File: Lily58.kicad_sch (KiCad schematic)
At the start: 40 parts, among them J1 USB_C_Receptacle, J2 USB_C_Receptacle, J3 Conn_01x03_Pin, U1 BQ24091DGQ, U2 TPS63000, U3 TPS63000

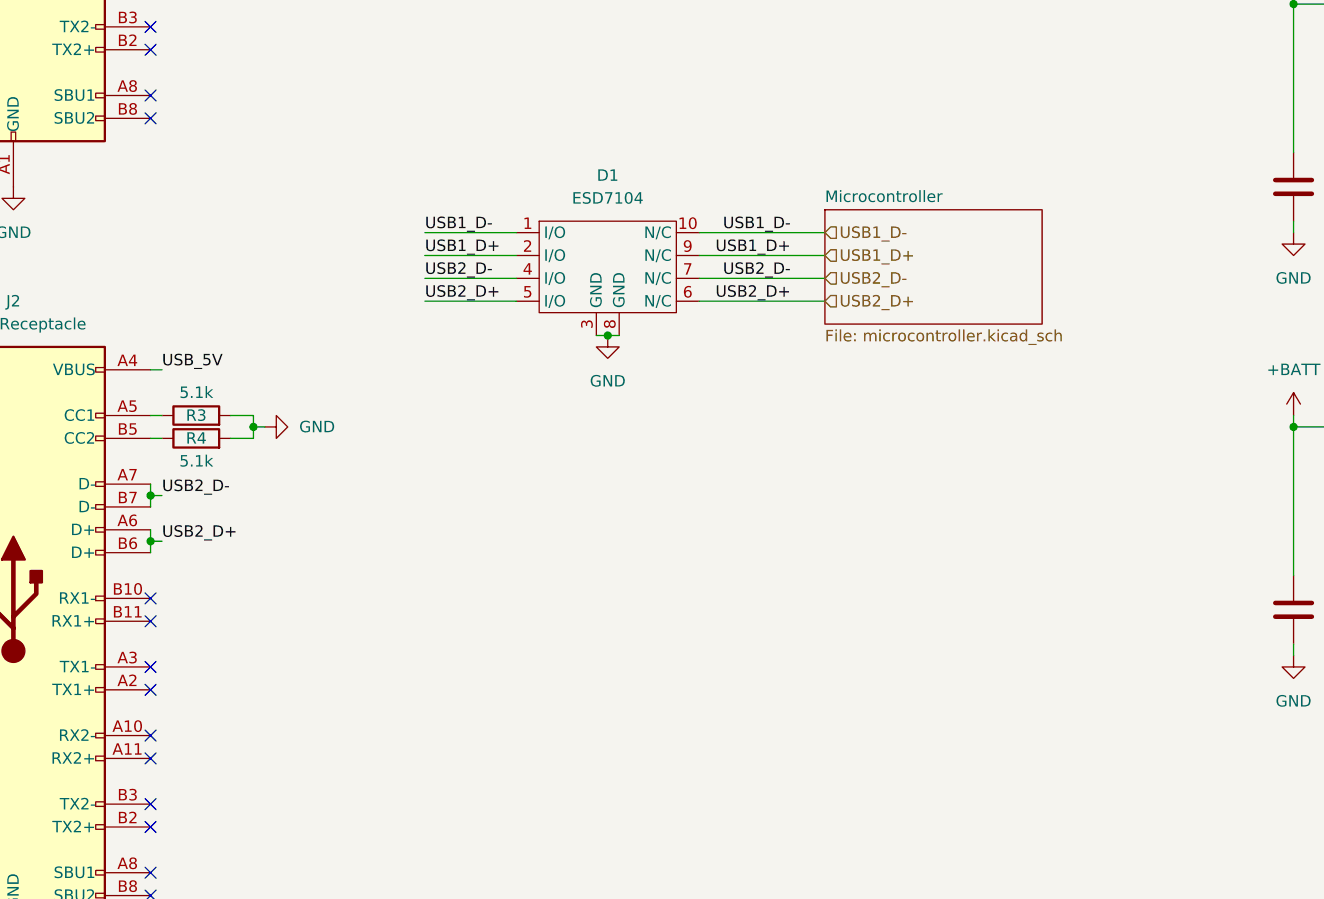
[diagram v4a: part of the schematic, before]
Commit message: completed ESP32-S3 circuit
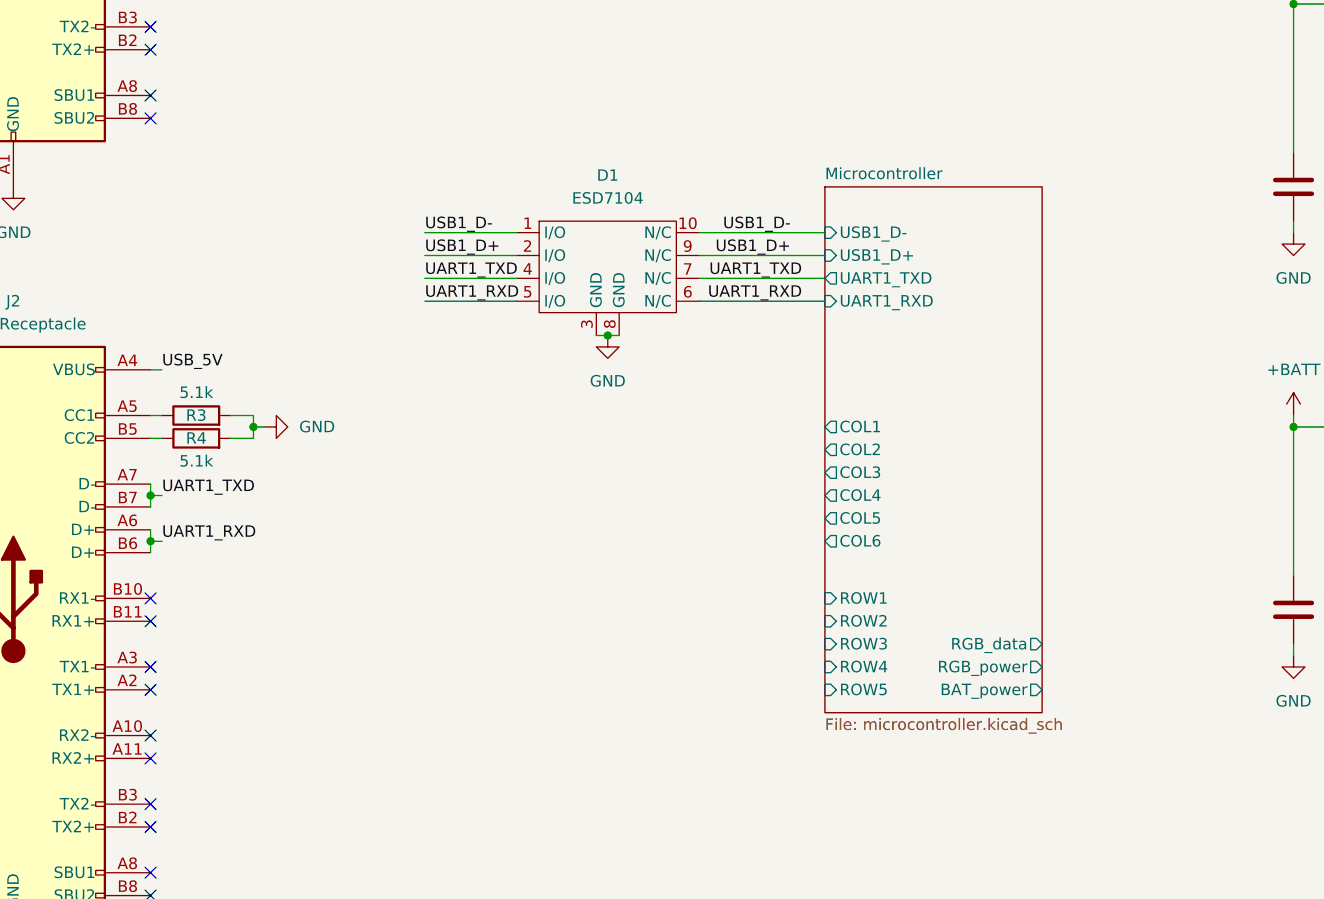
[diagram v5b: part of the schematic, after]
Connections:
- net USB2_D+ renamed UART1_RXD
- net USB2_D- renamed UART1_TXD
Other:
- sheet Microcontroller ports: added BAT_power, COL1, COL2, COL3, COL4, COL5, COL6, RGB_data, RGB_power, ROW1, ROW2, ROW3, ROW4, ROW5, UART1_RXD, UART1_TXD, USB1_D+, USB1_D-; removed none
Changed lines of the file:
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@@
     (effects (font (size 1.27 1.27)) (justify left bottom))
   )
-  (label "USB2_D-" (at 45.72 132.08 0) (fields_autoplaced)
+  (label "UART1_TXD" (at 45.72 132.08 0) (fields_autoplaced)
     (effects (font (size 1.27 1.27)) (justify left bottom))
   )
@@
     (effects (font (size 1.27 1.27)) (justify right bottom))
   )
-  (label "USB2_D+" (at 115.57 110.49 180) (fields_autoplaced)
+  (label "UART1_RXD" (at 116.84 110.49 180) (fields_autoplaced)
     (effects (font (size 1.27 1.27)) (justify right bottom))
   )
@@
     (effects (font (size 1.27 1.27)) (justify right bottom))
   )
-  (label "USB2_D-" (at 115.57 107.95 180) (fields_autoplaced)
+  (label "UART1_TXD" (at 116.84 107.95 180) (fields_autoplaced)
     (effects (font (size 1.27 1.27)) (justify right bottom))
   )
@@
     (effects (font (size 1.27 1.27)) (justify left bottom))
   )
-  (label "USB2_D-" (at 74.93 107.95 0) (fields_autoplaced)
+  (label "UART1_TXD" (at 74.93 107.95 0) (fields_autoplaced)
     (effects (font (size 1.27 1.27)) (justify left bottom))
   )
@@
     (effects (font (size 1.27 1.27)) (justify left bottom))
   )
-  (label "USB2_D+" (at 45.72 137.16 0) (fields_autoplaced)
+  (label "UART1_RXD" (at 45.72 137.16 0) (fields_autoplaced)
     (effects (font (size 1.27 1.27)) (justify left bottom))
   )
@@
     (effects (font (size 1.27 1.27)) (justify left bottom))
   )
-  (label "USB2_D+" (at 74.93 110.49 0) (fields_autoplaced)
+  (label "UART1_RXD" (at 74.93 110.49 0) (fields_autoplaced)
     (effects (font (size 1.27 1.27)) (justify left bottom))
-  )
-  (hierarchical_label "USB2_D-" (shape input) (at 119.38 107.95 0) (fields_autoplaced)
-    (effects (font (size 1.27 1.27)) (justify left))
-  )
-  (hierarchical_label "USB1_D-" (shape input) (at 119.38 102.87 0) (fields_autoplaced)
-    (effects (font (size 1.27 1.27)) (justify left))
-  )
-  (hierarchical_label "USB1_D+" (shape input) (at 119.38 105.41 0) (fields_autoplaced)
-    (effects (font (size 1.27 1.27)) (justify left))
-  )
-  (hierarchical_label "USB2_D+" (shape input) (at 119.38 110.49 0) (fields_autoplaced)
-    (effects (font (size 1.27 1.27)) (justify left))
   )
   (symbol (lib_id "power:GND") (at 215.9 102.87 0) (unit 1)
@@
     )
   )
-  (sheet (at 119.38 100.33) (size 24.13 12.7) (fields_autoplaced)
+  (sheet (at 119.38 97.79) (size 24.13 58.42) (fields_autoplaced)
     (stroke (width 0.1524) (type solid))
     (fill (color 0 0 0 0.0000))
-    (property "Sheetname" "Microcontroller" (at 119.38 99.6184 0)
+    (property "Sheetname" "Microcontroller" (at 119.38 97.0784 0)
       (effects (font (size 1.27 1.27)) (justify left bottom))
     )
-    (property "Sheetfile" "microcontroller.kicad_sch" (at 119.38 113.6146 0)
+    (property "Sheetfile" "microcontroller.kicad_sch" (at 119.38 156.7946 0)
       (effects (font (size 1.27 1.27)) (justify left top))
     )
-    (instances
+    (pin "ROW1" input (at 119.38 143.51 180)
+      (effects (font (size 1.27 1.27)) (justify left))
+    )
+    (pin "COL5" output (at 119.38 134.62 180)
+      (effects (font (size 1.27 1.27)) (justify left))
+    )
+    (pin "COL4" output (at 119.38 132.08 180)
+      (effects (font (size 1.27 1.27)) (justify left))
+    )
+    (pin "COL3" output (at 119.38 129.54 180)
+      (effects (font (size 1.27 1.27)) (justify left))
+    )
+    (pin "ROW3" input (at 119.38 148.59 180)
+      (effects (font (size 1.27 1.27)) (justify left))
+    )
+    (pin "ROW4" input (at 119.38 151.13 180)
+      (effects (font (size 1.27 1.27)) (justify left))
+    )
+    (pin "ROW2" input (at 119.38 146.05 180)
+      (effects (font (size 1.27 1.27)) (justify left))
+    )
+    (pin "COL2" output (at 119.38 127 180)
+      (effects (font (size 1.27 1.27)) (justify left))
+    )
+    (pin "COL1" output (at 119.38 124.46 180)
+      (effects (font (size 1.27 1.27)) (justify left))
+    )
+    (pin "USB1_D+" input (at 119.38 105.41 180)
+      (effects (font (size 1.27 1.27)) (justify left))
+    )
+    (pin "USB1_D-" input (at 119.38 102.87 180)
+      (effects (font (size 1.27 1.27)) (justify left))
+    )
+    (pin "UART1_RXD" input (at 119.38 110.49 180)
+      (effects (font (size 1.27 1.27)) (justify left))
+    )
+    (pin "UART1_TXD" output (at 119.38 107.95 180)
+      (effects (font (size 1.27 1.27)) (justify left))
+    )
+    (pin "COL6" output (at 119.38 137.16 180)
+      (effects (font (size 1.27 1.27)) (justify left))
+    )
+    (pin "ROW5" input (at 119.38 153.67 180)
+      (effects (font (size 1.27 1.27)) (justify left))
+    )
+    (pin "RGB_power" output (at 143.51 151.13 0)
+      (effects (font (size 1.27 1.27)) (justify right))
+    )
+    (pin "RGB_data" output (at 143.51 148.59 0)
+      (effects (font (size 1.27 1.27)) (justify right))
+    )
+    (pin "BAT_power" output (at 143.51 153.67 0)
+      (effects (font (size 1.27 1.27)) (justify right))
+    )
+    (instances

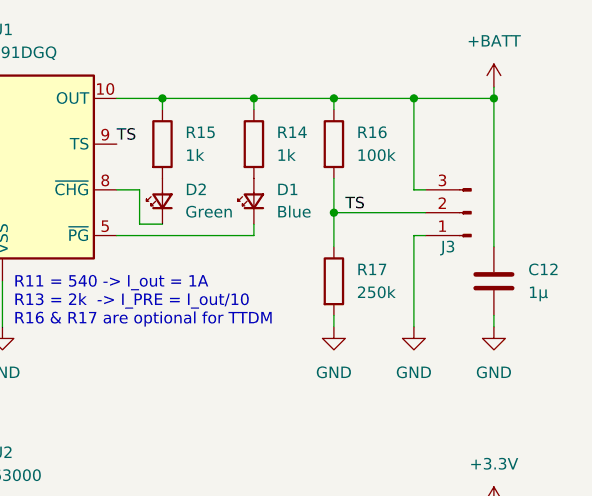
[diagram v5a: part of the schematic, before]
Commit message: added power switch
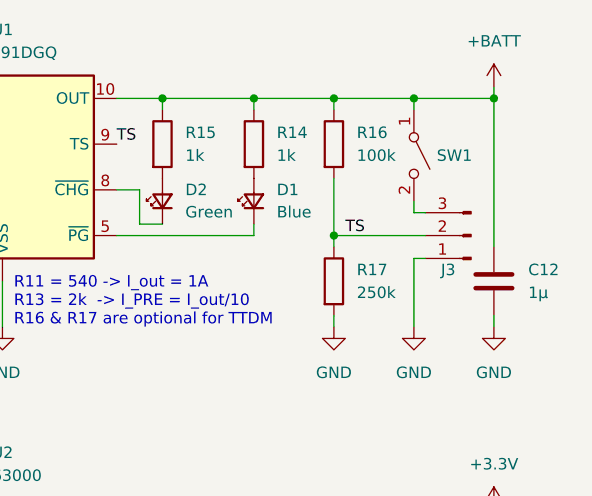
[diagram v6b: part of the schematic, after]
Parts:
- added SW1: SW_SPST, symbol Switch:SW_SPST
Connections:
- net +BATT: now also SW1.1 (A); no longer J3.3 (Pin_3)
- new net: J3.3 (Pin_3), SW1.2 (B)
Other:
- moved on the sheet: J3
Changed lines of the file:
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@@
   (junction (at 236.22 77.47) (diameter 0) (color 0 0 0 0)
   )
+  (junction (at 254 45.72) (diameter 0) (color 0 0 0 0)
+  )
   (junction (at 181.61 137.16) (diameter 0) (color 0 0 0 0)
   )
@@
   )
   (junction (at 236.22 124.46) (diameter 0) (color 0 0 0 0)
-  )
-  (junction (at 254 43.18) (diameter 0) (color 0 0 0 0)
   )
   (junction (at 236.22 137.16) (diameter 0) (color 0 0 0 0)
@@
     (stroke (width 0) (type default))
   )
-  (wire (pts (xy 262.89 40.64) (xy 264.16 40.64))
+  (wire (pts (xy 262.89 43.18) (xy 264.16 43.18))
     (stroke (width 0) (type default))
   )
@@
     (stroke (width 0) (type default))
   )
-  (wire (pts (xy 254 43.18) (xy 254 46.99))
-    (stroke (width 0) (type default))
-  )
   (wire (pts (xy 245.11 31.75) (xy 245.11 30.48))
     (stroke (width 0) (type default))
@@
     (stroke (width 0) (type default))
   )
+  (wire (pts (xy 262.89 41.91) (xy 262.89 43.18))
+    (stroke (width 0) (type default))
+  )
   (wire (pts (xy 247.65 90.17) (xy 236.22 90.17))
     (stroke (width 0) (type default))
@@
     (stroke (width 0) (type default))
   )
-  (wire (pts (xy 254 39.37) (xy 254 43.18))
+  (wire (pts (xy 254 39.37) (xy 254 45.72))
     (stroke (width 0) (type default))
   )
@@
     (stroke (width 0) (type default))
   )
-  (wire (pts (xy 262.89 45.72) (xy 264.16 45.72))
+  (wire (pts (xy 262.89 48.26) (xy 264.16 48.26))
     (stroke (width 0) (type default))
   )
@@
     (stroke (width 0) (type default))
   )
-  (wire (pts (xy 262.89 45.72) (xy 262.89 55.88))
+  (wire (pts (xy 262.89 48.26) (xy 262.89 55.88))
     (stroke (width 0) (type default))
   )
@@
     (stroke (width 0) (type default))
   )
-  (wire (pts (xy 254 43.18) (xy 264.16 43.18))
+  (wire (pts (xy 254 45.72) (xy 264.16 45.72))
     (stroke (width 0) (type default))
   )
@@
     (stroke (width 0) (type default))
   )
+  (wire (pts (xy 254 45.72) (xy 254 46.99))
+    (stroke (width 0) (type default))
+  )
   (wire (pts (xy 55.88 39.37) (xy 53.34 39.37))
     (stroke (width 0) (type default))
   )
-  (wire (pts (xy 262.89 30.48) (xy 262.89 40.64))
+  (wire (pts (xy 262.89 30.48) (xy 262.89 31.75))
     (stroke (width 0) (type default))
   )
@@
     (effects (font (size 1.27 1.27)) (justify left bottom))
   )
-  (label "TS" (at 255.27 43.18 0) (fields_autoplaced)
+  (label "TS" (at 255.27 45.72 0) (fields_autoplaced)
     (effects (font (size 1.27 1.27)) (justify left bottom))
   )
@@
     )
   )
-  (symbol (lib_id "Connector:Conn_01x03_Pin") (at 269.24 43.18 180) (unit 1)
+  (symbol (lib_id "Connector:Conn_01x03_Pin") (at 269.24 45.72 180) (unit 1)
     (in_bom yes) (on_board yes) (dnp no)
-    (property "Reference" "J3" (at 266.7 46.99 0)
-      (effects (font (size 1.27 1.27)))
-    )
-    (property "Value" "Conn_01x03_Pin" (at 268.605 48.26 0)
-      (effects (font (size 1.27 1.27)) hide)
-    )
-    (property "Footprint" "" (at 269.24 43.18 0)
-      (effects (font (size 1.27 1.27)) hide)
-    )
-    (property "Datasheet" "~" (at 269.24 43.18 0)
+    (property "Reference" "J3" (at 266.7 49.53 0)
+      (effects (font (size 1.27 1.27)))
+    )
+    (property "Value" "Conn_01x03_Pin" (at 268.605 50.8 0)
+      (effects (font (size 1.27 1.27)) hide)
+    )
+    (property "Footprint" "" (at 269.24 45.72 0)
+      (effects (font (size 1.27 1.27)) hide)
+    )
+    (property "Datasheet" "~" (at 269.24 45.72 0)
       (effects (font (size 1.27 1.27)) hide)
     )
@@
         )
       )
+    )
+  )
+  (symbol (lib_id "Switch:SW_SPST") (at 262.89 36.83 270) (unit 1)
+    (in_bom yes) (on_board yes) (dnp no) (fields_autoplaced)
+    (property "Reference" "SW1" (at 265.43 36.83 90)
+      (effects (font (size 1.27 1.27)) (justify left))
+    )
+    (property "Value" "SW_SPST" (at 265.43 38.1 90)
+      (effects (font (size 1.27 1.27)) (justify left) hide)
+    )
+    (property "Footprint" "" (at 262.89 36.83 0)
+      (effects (font (size 1.27 1.27)) hide)
+    )
+    (property "Datasheet" "~" (at 262.89 36.83 0)
+      (effects (font (size 1.27 1.27)) hide)
+    )
+    (pin "1")
+    (pin "2")
+    (instances
+      (project "Lily58"
+        (path "/a0958e12-2248-4ac3-b259-3086ac296b70"
+          (reference "SW1") (unit 1)
+        )
+      )

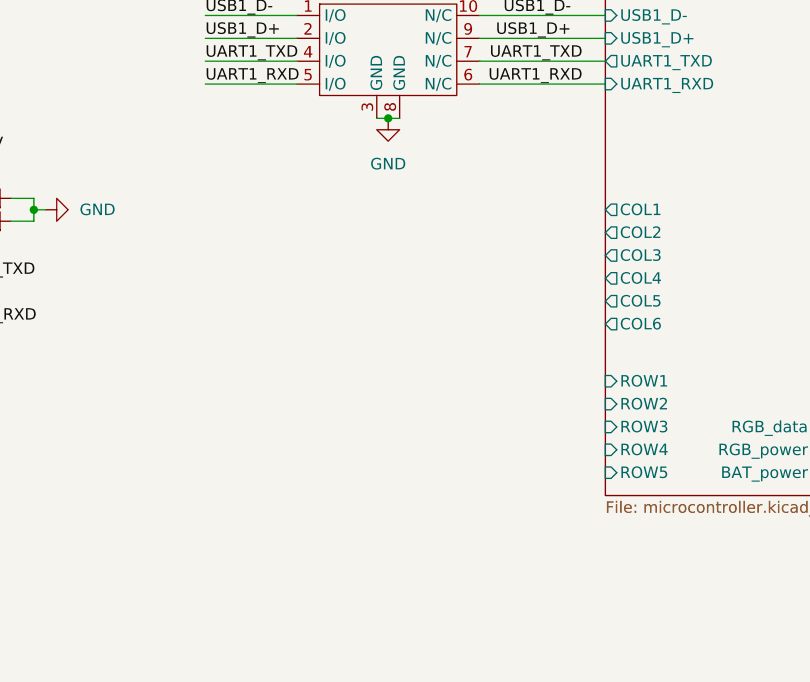
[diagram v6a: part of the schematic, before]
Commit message: added base structure for switch matrix
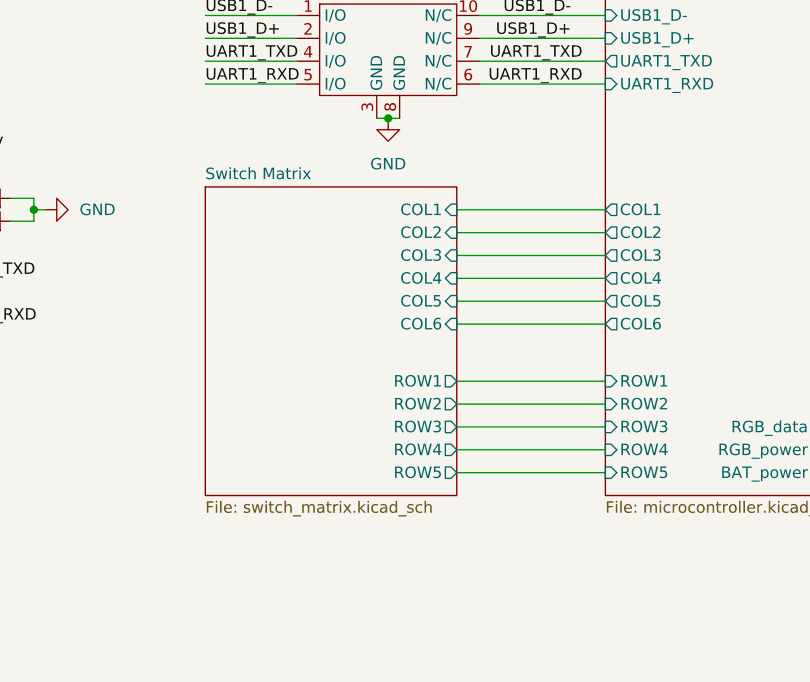
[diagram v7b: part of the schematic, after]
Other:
- added sheet Switch Matrix (switch_matrix.kicad_sch)
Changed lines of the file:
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@@
+    (stroke (width 0) (type default))
+  )
+  (wire (pts (xy 102.87 143.51) (xy 119.38 143.51))
     (stroke (width 0) (type default))
   )
@@
     (stroke (width 0) (type default))
   )
+  (wire (pts (xy 102.87 151.13) (xy 119.38 151.13))
+    (stroke (width 0) (type default))
+  )
   (wire (pts (xy 53.34 123.19) (xy 55.88 123.19))
     (stroke (width 0) (type default))
   )
+  (wire (pts (xy 102.87 146.05) (xy 119.38 146.05))
+    (stroke (width 0) (type default))
+  )
   (wire (pts (xy 207.01 134.62) (xy 200.66 134.62))
     (stroke (width 0) (type default))
@@
     (stroke (width 0) (type default))
   )
+  (wire (pts (xy 102.87 129.54) (xy 119.38 129.54))
+    (stroke (width 0) (type default))
+  )
   (wire (pts (xy 236.22 90.17) (xy 236.22 93.98))
     (stroke (width 0) (type default))
@@
     (stroke (width 0) (type default))
   )
+  (wire (pts (xy 102.87 148.59) (xy 119.38 148.59))
+    (stroke (width 0) (type default))
+  )
   (wire (pts (xy 236.22 133.35) (xy 236.22 137.16))
     (stroke (width 0) (type default))
@@
     (stroke (width 0) (type default))
   )
+  (wire (pts (xy 102.87 124.46) (xy 119.38 124.46))
+    (stroke (width 0) (type default))
+  )
   (wire (pts (xy 199.39 45.72) (xy 199.39 46.99))
     (stroke (width 0) (type default))
@@
     (stroke (width 0) (type default))
   )
+  (wire (pts (xy 102.87 134.62) (xy 119.38 134.62))
+    (stroke (width 0) (type default))
+  )
   (wire (pts (xy 245.11 44.45) (xy 245.11 45.72))
     (stroke (width 0) (type default))
   )
+  (wire (pts (xy 102.87 132.08) (xy 119.38 132.08))
+    (stroke (width 0) (type default))
+  )
   (wire (pts (xy 181.61 137.16) (xy 181.61 140.97))
     (stroke (width 0) (type default))
@@
     (stroke (width 0) (type default))
   )
+  (wire (pts (xy 102.87 153.67) (xy 119.38 153.67))
+    (stroke (width 0) (type default))
+  )
   (wire (pts (xy 171.45 77.47) (xy 171.45 93.98))
     (stroke (width 0) (type default))
@@
     (stroke (width 0) (type default))
   )
+  (wire (pts (xy 102.87 127) (xy 119.38 127))
+    (stroke (width 0) (type default))
+  )
   (wire (pts (xy 189.23 82.55) (xy 207.01 82.55))
     (stroke (width 0) (type default))
@@
   )
   (wire (pts (xy 254 45.72) (xy 264.16 45.72))
+    (stroke (width 0) (type default))
+  )
+  (wire (pts (xy 102.87 137.16) (xy 119.38 137.16))
     (stroke (width 0) (type default))
   )
@@
       )
     )
+  )
+  (sheet (at 74.93 121.92) (size 27.94 34.29) (fields_autoplaced)
+    (stroke (width 0.1524) (type solid))
+    (fill (color 0 0 0 0.0000))
+    (property "Sheetname" "Switch Matrix" (at 74.93 121.2084 0)
+      (effects (font (size 1.27 1.27)) (justify left bottom))
+    )
+    (property "Sheetfile" "switch_matrix.kicad_sch" (at 74.93 156.7946 0)
+      (effects (font (size 1.27 1.27)) (justify left top))
+    )
+    (pin "ROW3" output (at 102.87 148.59 0)
+      (effects (font (size 1.27 1.27)) (justify right))
+    )
+    (pin "ROW2" output (at 102.87 146.05 0)
+      (effects (font (size 1.27 1.27)) (justify right))
+    )
+    (pin "ROW4" output (at 102.87 151.13 0)
+      (effects (font (size 1.27 1.27)) (justify right))
+    )
+    (pin "ROW1" output (at 102.87 143.51 0)
+      (effects (font (size 1.27 1.27)) (justify right))
+    )
+    (pin "ROW5" output (at 102.87 153.67 0)
+      (effects (font (size 1.27 1.27)) (justify right))
+    )
+    (pin "COL3" input (at 102.87 129.54 0)
+      (effects (font (size 1.27 1.27)) (justify right))
+    )
+    (pin "COL4" input (at 102.87 132.08 0)
+      (effects (font (size 1.27 1.27)) (justify right))
+    )
+    (pin "COL5" input (at 102.87 134.62 0)
+      (effects (font (size 1.27 1.27)) (justify right))
+    )
+    (pin "COL6" input (at 102.87 137.16 0)
+      (effects (font (size 1.27 1.27)) (justify right))
+    )
+    (pin "COL1" input (at 102.87 124.46 0)
+      (effects (font (size 1.27 1.27)) (justify right))
+    )
+    (pin "COL2" input (at 102.87 127 0)
+      (effects (font (size 1.27 1.27)) (justify right))
+    )
+    (instances
+      (project "Lily58"
+        (path "/a0958e12-2248-4ac3-b259-3086ac296b70" (page "3"))
+      )
+    )
